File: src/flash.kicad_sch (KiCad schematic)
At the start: 17 parts, among them J2 Micro_SD_Card_Det1, U1 ECP5U_12_CABGA256, U11 W25Q128JVS

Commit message: Rev 2
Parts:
- C22: LCSC Part (none) -> C59461; MNF1_URL www.yageo.com -> (none); MPN CC0805ZKY5V5BB226 -> (none)
- C25: LCSC Part (none) -> C19702
- C26, C41: LCSC Part (none) -> C1525
- R16, R17, R24: LCSC Part (none) -> C23162; MNF1_URL www.yageo.com -> (none); MPN AC0603FR-104K7L -> (none)
- R18: LCSC Part (none) -> C21190
- R19: Digikey 311-10KLMCT-ND -> (none); Koncar FR013 -> (none); LCSC C15401 -> (none); LCSC Part (none) -> C25804; MNF1_URL www.yageo.com -> (none); MPN RC0603FR-0710KL -> (none); Mouser 603-RC0603FR-0710KL -> (none); Newark 94X1379 -> (none)
- R20, R21, R22: LCSC Part (none) -> C25804
- R23: LCSC Part (none) -> C23162; MPN RC0402JR-075K1L -> (none); Manufacturer Yageo -> (none); Manufacturer2 UNI-ROYAL(Uniroyal Elec) -> (none)
- R38: Digikey 73L2R47JCT-ND -> (none); Koncar FR001 -> (none); LCSC C158884 -> (none); LCSC Part (none) -> C3013349; MFG1 CTS -> (none); MNF1_URL www.ctscorp.com -> (none); MPN 73L2R47J -> (none); Mouser 774-73L2R47J -> (none); Newark 32K1357 -> (none)
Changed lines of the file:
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@@
+			)
+		)
+		(property "LCSC Part" "C25804"
+			(at 114.3 82.55 0)
+			(effects
+				(font
+					(size 1.27 1.27)
+				)
 			)
 		)
@@
 			)
 		)
+		(property "LCSC Part" "C25804"
+			(at 119.38 82.55 0)
+			(effects
+				(font
+					(size 1.27 1.27)
+				)
+			)
+		)
 		(pin "1"
 		)
@@
 			)
 		)
+		(property "LCSC Part" "C21190"
+			(at 137.16 57.15 0)
+			(effects
+				(font
+					(size 1.27 1.27)
+				)
+			)
+		)
 		(pin "1"
 		)
@@
 			)
 		)
-		(property "MNF1_URL" "www.yageo.com"
-			(at 129.54 82.55 90)
-			(effects
-				(font
-					(size 1.27 1.27)
-				)
-				(hide yes)
-			)
-		)
-		(property "MPN" "AC0603FR-104K7L"
-			(at 129.54 82.55 90)
-			(effects
-				(font
-					(size 1.27 1.27)
-				)
-				(hide yes)
+		(property "LCSC Part" "C23162"
+			(at 129.54 82.55 0)
+			(effects
+				(font
+					(size 1.27 1.27)
+				)
 			)
 		)
@@
 			)
 		)
+		(property "LCSC Part" "C25804"
+			(at 109.22 82.55 0)
+			(effects
+				(font
+					(size 1.27 1.27)
+				)
+			)
+		)
 		(pin "1"
 		)
@@
 			)
 		)
-		(property "MFG1" "CTS"
-			(at 35.56 140.97 90)
-			(effects
-				(font
-					(size 1.27 1.27)
-				)
-				(hide yes)
-			)
-		)
-		(property "MNF1_URL" "www.ctscorp.com"
-			(at 35.56 140.97 90)
-			(effects
-				(font
-					(size 1.27 1.27)
-				)
-				(hide yes)
-			)
-		)
-		(property "MPN" "73L2R47J"
-			(at 35.56 140.97 90)
-			(effects
-				(font
-					(size 1.27 1.27)
-				)
-				(hide yes)
-			)
-		)
-		(property "Mouser" "774-73L2R47J"
-			(at 35.56 140.97 90)
-			(effects
-				(font
-					(size 1.27 1.27)
-				)
-				(hide yes)
-			)
-		)
-		(property "Digikey" "73L2R47JCT-ND"
-			(at 35.56 140.97 90)
-			(effects
-				(font
-					(size 1.27 1.27)
-				)
-				(hide yes)
-			)
-		)
-		(property "Newark" "32K1357"
-			(at 35.56 140.97 90)
-			(effects
-				(font
-					(size 1.27 1.27)
-				)
-				(hide yes)
-			)
-		)
-		(property "LCSC" "C158884"
-			(at 35.56 140.97 90)
-			(effects
-				(font
-					(size 1.27 1.27)
-				)
-				(hide yes)
-			)
-		)
-		(property "Koncar" "FR001"
-			(at 35.56 140.97 90)
-			(effects
-				(font
-					(size 1.27 1.27)
-				)
-				(hide yes)
+		(property "LCSC Part" "C3013349"
+			(at 35.56 140.97 0)
+			(effects
+				(font
+					(size 1.27 1.27)
+				)
 			)
 		)
@@
 			)
 		)
-		(property "LCSC Part" ""
+		(property "LCSC Part" "C19702"
 			(at 156.21 45.72 0)
 			(effects
@@
 			)
 		)
-		(property "MNF1_URL" "www.yageo.com"
-			(at 119.38 54.61 90)
-			(effects
-				(font
-					(size 1.27 1.27)
-				)
-				(hide yes)
-			)
-		)
-		(property "MPN" "AC0603FR-104K7L"
-			(at 119.38 54.61 90)
-			(effects
-				(font
-					(size 1.27 1.27)
-				)
-				(hide yes)
+		(property "LCSC Part" "C23162"
+			(at 119.38 54.61 0)
+			(effects
+				(font
+					(size 1.27 1.27)
+				)
 			)
 		)
@@
 			)
 		)
-		(property "MNF1_URL" "www.yageo.com"
-			(at 124.46 54.61 90)
-			(effects
-				(font
-					(size 1.27 1.27)
-				)
-				(hide yes)
-			)
-		)
-		(property "MPN" "AC0603FR-104K7L"
-			(at 124.46 54.61 90)
-			(effects
-				(font
-					(size 1.27 1.27)
-				)
-				(hide yes)
+		(property "LCSC Part" "C23162"
+			(at 124.46 54.61 0)
+			(effects
+				(font
+					(size 1.27 1.27)
+				)
 			)
 		)
@@
 			)
 		)
-		(property "LCSC Part" ""
+		(property "LCSC Part" "C1525"
 			(at 179.07 45.72 0)
 			(effects
@@
 			)
 		)
-		(property "MNF1_URL" "www.yageo.com"
+		(property "LCSC Part" "C59461"
 			(at 35.56 151.13 0)
 			(effects
@@
 					(size 1.27 1.27)
 				)
-				(hide yes)
-			)
-		)
-		(property "MPN" "CC0805ZKY5V5BB226 "
-			(at 35.56 151.13 0)
-			(effects
-				(font
-					(size 1.27 1.27)
-				)
-				(hide yes)
 			)
 		)
@@
 			)
 		)
-		(property "MNF1_URL" "www.yageo.com"
-			(at 104.14 82.55 90)
-			(effects
-				(font
-					(size 1.27 1.27)
-				)
-				(hide yes)
-			)
-		)
-		(property "MPN" "RC0603FR-0710KL"
-			(at 104.14 82.55 90)
-			(effects
-				(font
-					(size 1.27 1.27)
-				)
-				(hide yes)
-			)
-		)
-		(property "Mouser" "603-RC0603FR-0710KL"
-			(at 104.14 82.55 90)
-			(effects
-				(font
-					(size 1.27 1.27)
-				)
-				(hide yes)
-			)
-		)
-		(property "Digikey" "311-10KLMCT-ND"
-			(at 104.14 82.55 90)
-			(effects
-				(font
-					(size 1.27 1.27)
-				)
-				(hide yes)
-			)
-		)
-		(property "Newark" "94X1379"
-			(at 104.14 82.55 90)
-			(effects
-				(font
-					(size 1.27 1.27)
-				)
-				(hide yes)
-			)
-		)
-		(property "LCSC" "C15401"
-			(at 104.14 82.55 90)
-			(effects
-				(font
-					(size 1.27 1.27)
-				)
-				(hide yes)
-			)
-		)
-		(property "Koncar" "FR013"
-			(at 104.14 82.55 90)
-			(effects
-				(font
-					(size 1.27 1.27)
-				)
-				(hide yes)
+		(property "LCSC Part" "C25804"
+			(at 104.14 82.55 0)
+			(effects
+				(font
+					(size 1.27 1.27)
+				)
 			)
 		)
@@
 			)
 		)
-		(property "LCSC Part" ""
+		(property "LCSC Part" "C1525"
 			(at 167.64 45.72 0)
 			(effects
@@
 			)
 		)
-		(property "DNP" ""
-			(at 125.73 83.82 0)
-			(effects
-				(font
-					(size 1.27 1.27)
-				)
-				(justify left top)
-			)
-		)
-		(property "MPN" "RC0402JR-075K1L\n"
+		(property "LCSC Part" "C23162"
 			(at 124.46 82.55 0)
 			(effects
-				(font
-					(size 1.27 1.27)
-				)
-				(hide yes)
-			)
-		)
-		(property "Manufacturer" "Yageo"
-			(at 124.46 82.55 0)
-			(effects
-				(font
-					(size 1.27 1.27)
-				)
-				(hide yes)
-			)
-		)
-		(property "Manufacturer2" "UNI-ROYAL(Uniroyal Elec)"
-			(at 124.46 82.55 0)
-			(effects
-				(font
-					(size 1.27 1.27)
-				)
-				(hide yes)
-			)
-		)
-		(property "LCSC Part" ""
-			(at 124.46 82.55 0)
-			(effects

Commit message: Tidy project
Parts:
- C22: JLCPCB Part # (none) -> C59461; LCSC Part C59461 -> (none)
- C25: JLCPCB Part # (none) -> C19702; LCSC Part C19702 -> (none)
- C26, C41: JLCPCB Part # (none) -> C1525; LCSC Part C1525 -> (none)
- J2: JLCPCB Part # (none) -> C20613194; LCSC Part C20613194 -> (none)
- R16, R17, R23, R24: JLCPCB Part # (none) -> C23162; LCSC Part C23162 -> (none)
- R18: JLCPCB Part # (none) -> C21190; LCSC Part C21190 -> (none)
- R19, R20, R21, R22: JLCPCB Part # (none) -> C25804; LCSC Part C25804 -> (none)
- R38: JLCPCB Part # (none) -> C3013349; LCSC Part C3013349 -> (none)
- U1: JLCPCB Part # (none) -> C1521614; LCSC Part C1521614 -> (none)
- U11: JLCPCB Part # (none) -> C97521; LCSC Part C97521 -> (none)
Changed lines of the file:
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@@
 			)
 		)
-		(property "LCSC Part" "C25804"
+		(property "JLCPCB Part #" "C25804"
 			(at 114.3 82.55 0)
 			(effects
@@
 			)
 		)
-		(property "LCSC Part" "C25804"
+		(property "JLCPCB Part #" "C25804"
 			(at 119.38 82.55 0)
 			(effects
@@
 			)
 		)
-		(property "LCSC Part" "C21190"
+		(property "JLCPCB Part #" "C21190"
 			(at 137.16 57.15 0)
 			(effects
@@
 			)
 		)
-		(property "LCSC Part" "C23162"
+		(property "JLCPCB Part #" "C23162"
 			(at 129.54 82.55 0)
 			(effects
@@
 			)
 		)
-		(property "LCSC Part" "C25804"
+		(property "JLCPCB Part #" "C25804"
 			(at 109.22 82.55 0)
 			(effects
@@
 			)
 		)
-		(property "LCSC Part" "C3013349"
+		(property "JLCPCB Part #" "C3013349"
 			(at 35.56 140.97 0)
 			(effects
@@
 			)
 		)
-		(property "LCSC Part" "C20613194"
+		(property "JLCPCB Part #" "C20613194"
 			(at 81.28 148.59 0)
 			(effects
@@
 					(size 1.27 1.27)
 				)
-				(hide yes)
 			)
 		)
@@
 			)
 		)
-		(property "LCSC Part" "C19702"
+		(property "JLCPCB Part #" "C19702"
 			(at 156.21 45.72 0)
 			(effects
@@
 					(size 1.27 1.27)
 				)
-				(hide yes)
 			)
 		)
@@
 			)
 		)
-		(property "LCSC Part" "C23162"
+		(property "JLCPCB Part #" "C23162"
 			(at 119.38 54.61 0)
 			(effects
@@
 			)
 		)
-		(property "LCSC Part" "C23162"
+		(property "JLCPCB Part #" "C23162"
 			(at 124.46 54.61 0)
 			(effects
@@
 			)
 		)
-		(property "LCSC Part" " C1521614"
+		(property "JLCPCB Part #" " C1521614"
 			(at 171.45 95.25 0)
 			(effects
@@
 					(size 1.27 1.27)
 				)
-				(hide yes)
 			)
 		)
@@
 			)
 		)
-		(property "LCSC Part" "C1525"
+		(property "JLCPCB Part #" "C1525"
 			(at 179.07 45.72 0)
 			(effects
@@
 					(size 1.27 1.27)
 				)
-				(hide yes)
 			)
 		)
@@
 			)
 		)
-		(property "LCSC Part" " C97521"
+		(property "JLCPCB Part #" " C97521"
 			(at 163.83 140.97 0)
 			(effects
@@
 					(size 1.27 1.27)
 				)
-				(hide yes)
 			)
 		)
@@
 			)
 		)
-		(property "LCSC Part" "C59461"
+		(property "JLCPCB Part #" "C59461"
 			(at 35.56 151.13 0)
 			(effects
@@
 			)
 		)
-		(property "LCSC Part" "C25804"
+		(property "JLCPCB Part #" "C25804"
 			(at 104.14 82.55 0)
 			(effects
@@
 			)
 		)
-		(property "LCSC Part" "C1525"
+		(property "JLCPCB Part #" "C1525"
 			(at 167.64 45.72 0)
 			(effects
@@
 					(size 1.27 1.27)
 				)
-				(hide yes)
 			)
 		)
@@
 			)
 		)
-		(property "LCSC Part" "C23162"
+		(property "JLCPCB Part #" "C23162"
 			(at 124.46 82.55 0)
 			(effects
@@
 					(size 1.27 1.27)
 				)
-				(hide yes)
-			)
-		)
+			)
+		)

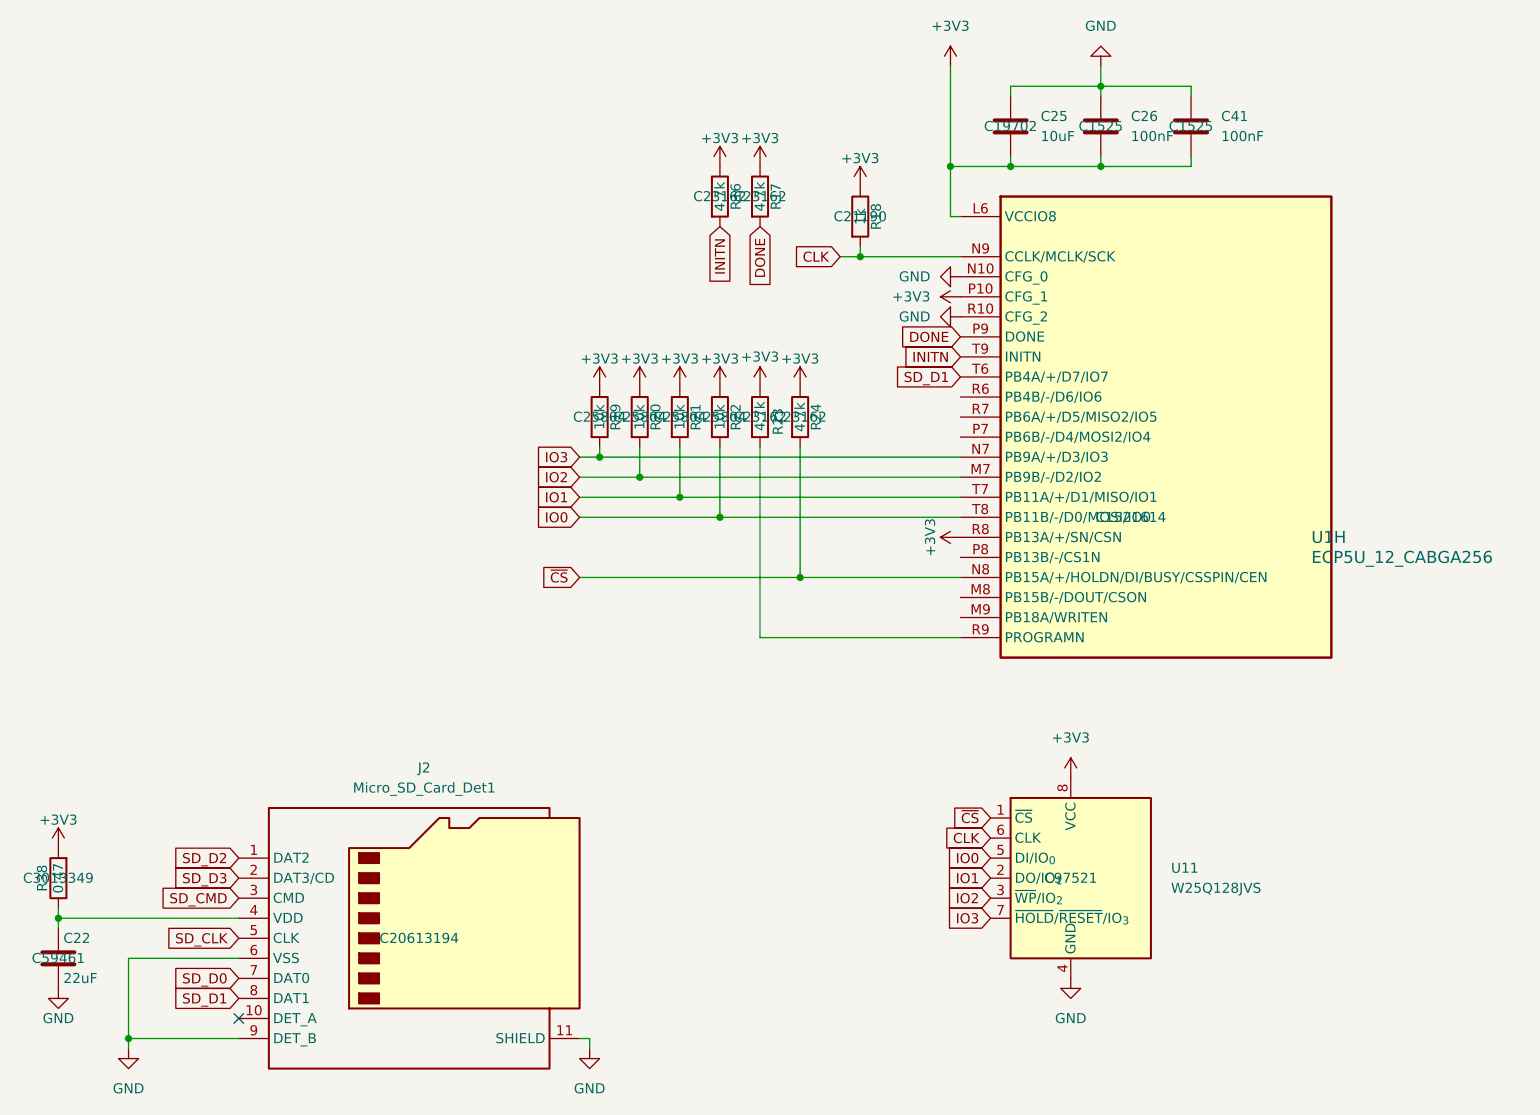
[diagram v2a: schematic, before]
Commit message: Add test points
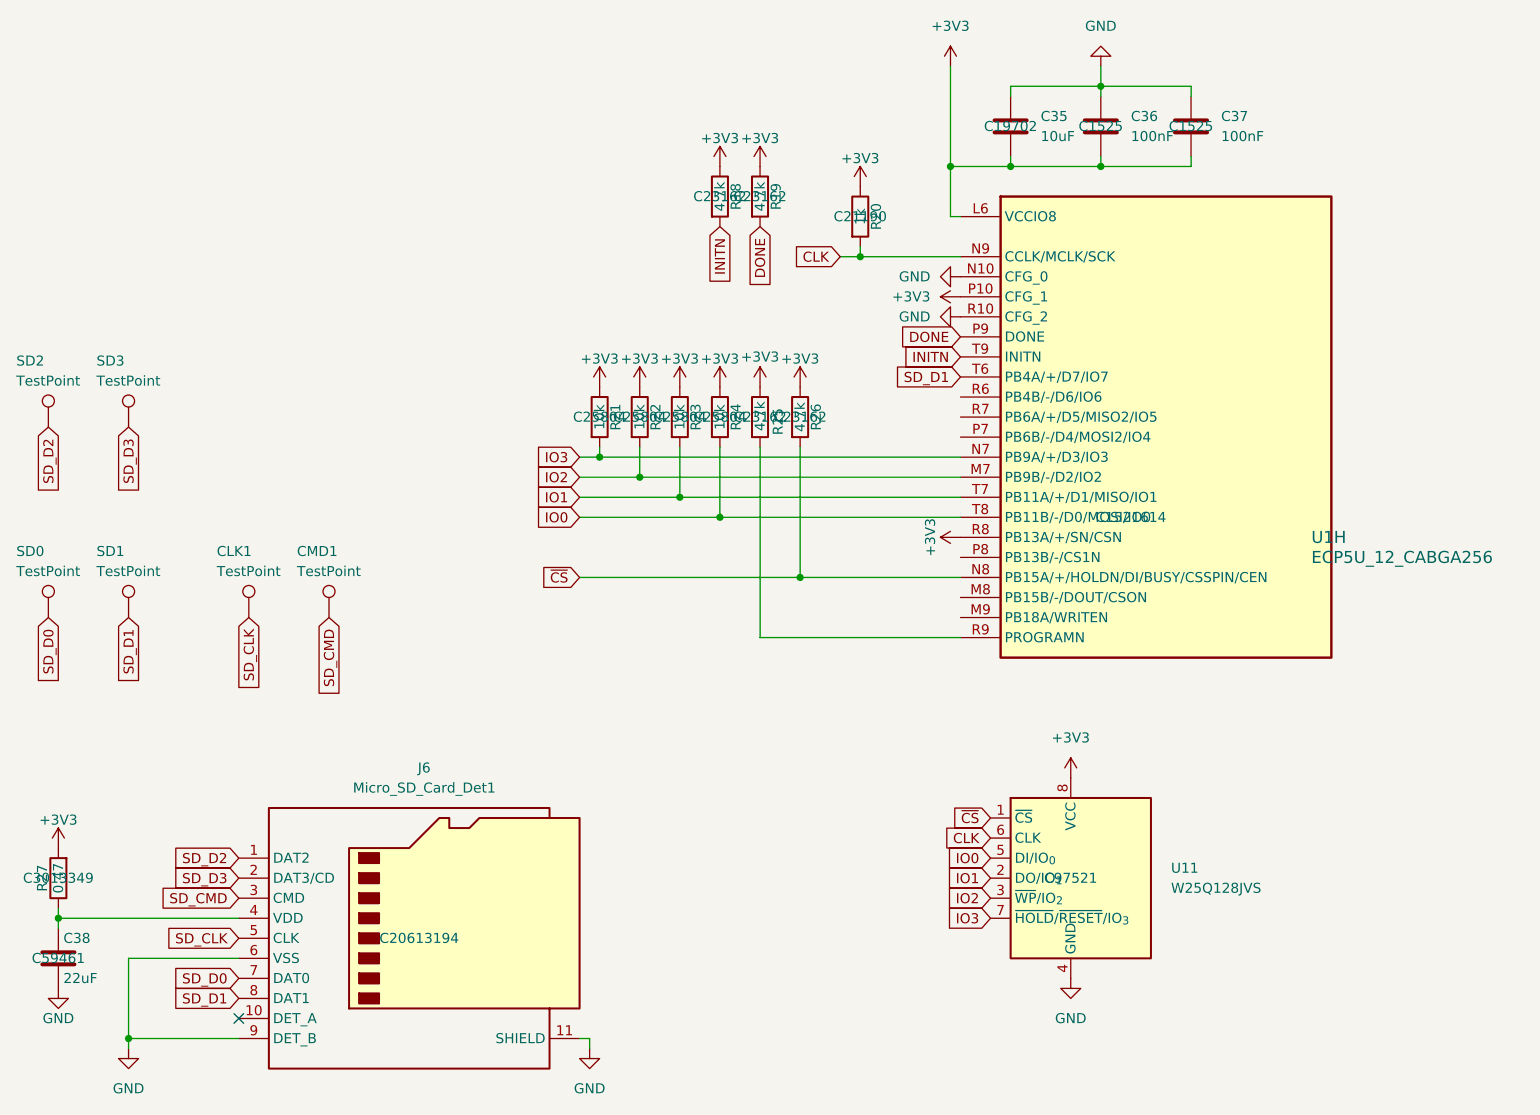
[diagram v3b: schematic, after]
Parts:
- added CLK1, CMD1, SD0, SD1, SD2, SD3: TestPoint, TestPoint:TestPoint_Pad_D1.5mm, symbol Connector:TestPoint
- renumbered C25 to C35, C26 to C36, C41 to C37, C22 to C38, J2 to J6, R16 to R18, R17 to R19, R18 to R20, R19 to R21, R20 to R22, R21 to R23, R22 to R24, R23 to R25, R24 to R26, R38 to R27
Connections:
- net SD_CLK: now also CLK1.1
- net SD_CMD: now also CMD1.1
- net SD_D0: now also SD0.1
- net SD_D1: now also SD1.1
- net SD_D2: now also SD2.1
- net SD_D3: now also SD3.1
